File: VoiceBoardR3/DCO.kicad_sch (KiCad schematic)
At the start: 74 parts, among them Q201 BC857, Q202 BC857, U201 TL074, U202 TL074, U203 MCP4451-104E-ST, U204 TL074, U205 MCP4451-104E-ST, U206 TL072

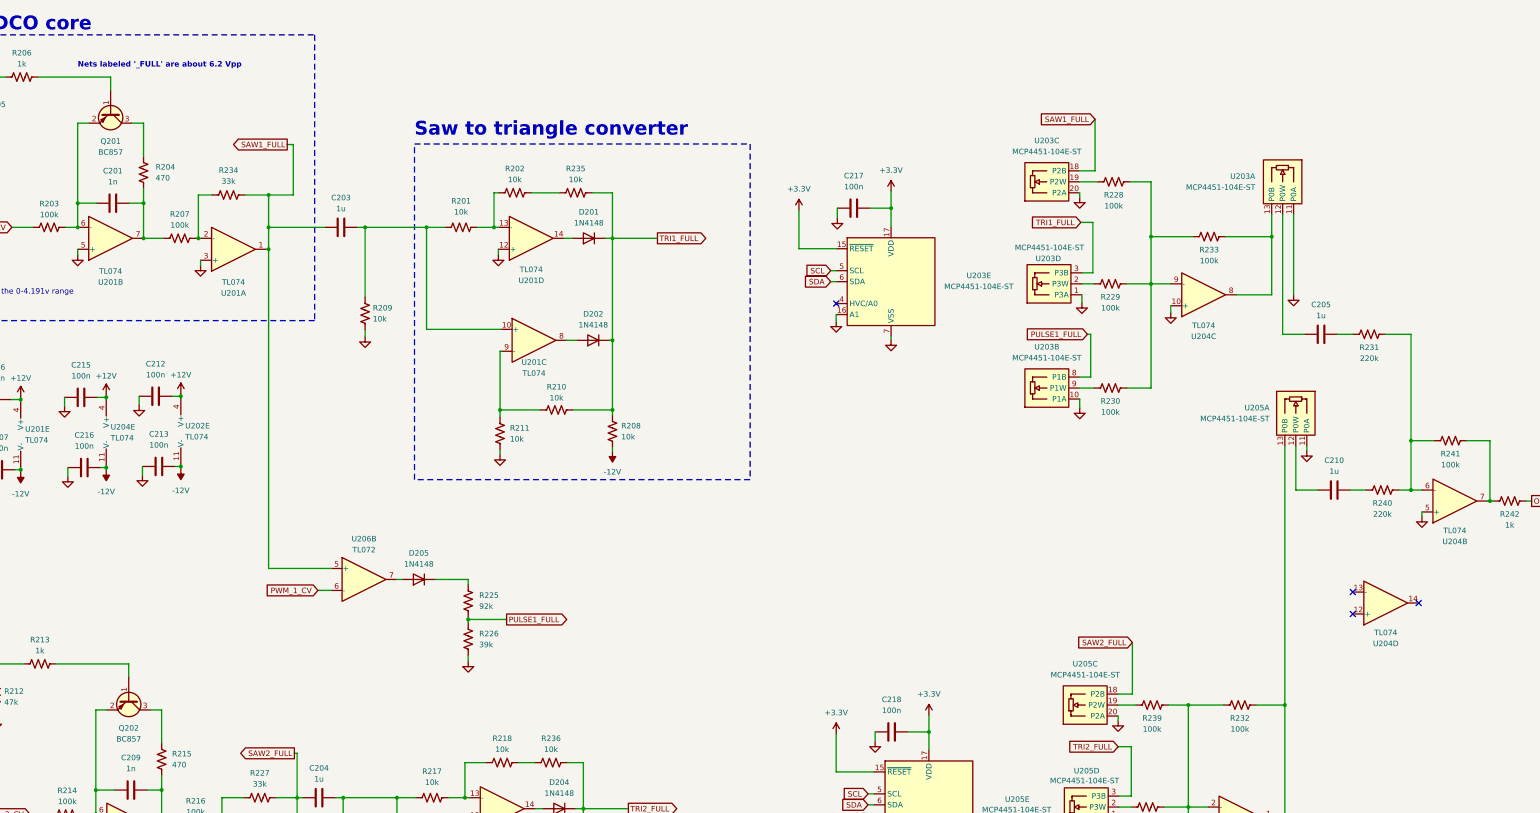
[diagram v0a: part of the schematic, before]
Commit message: updated to kicad 8
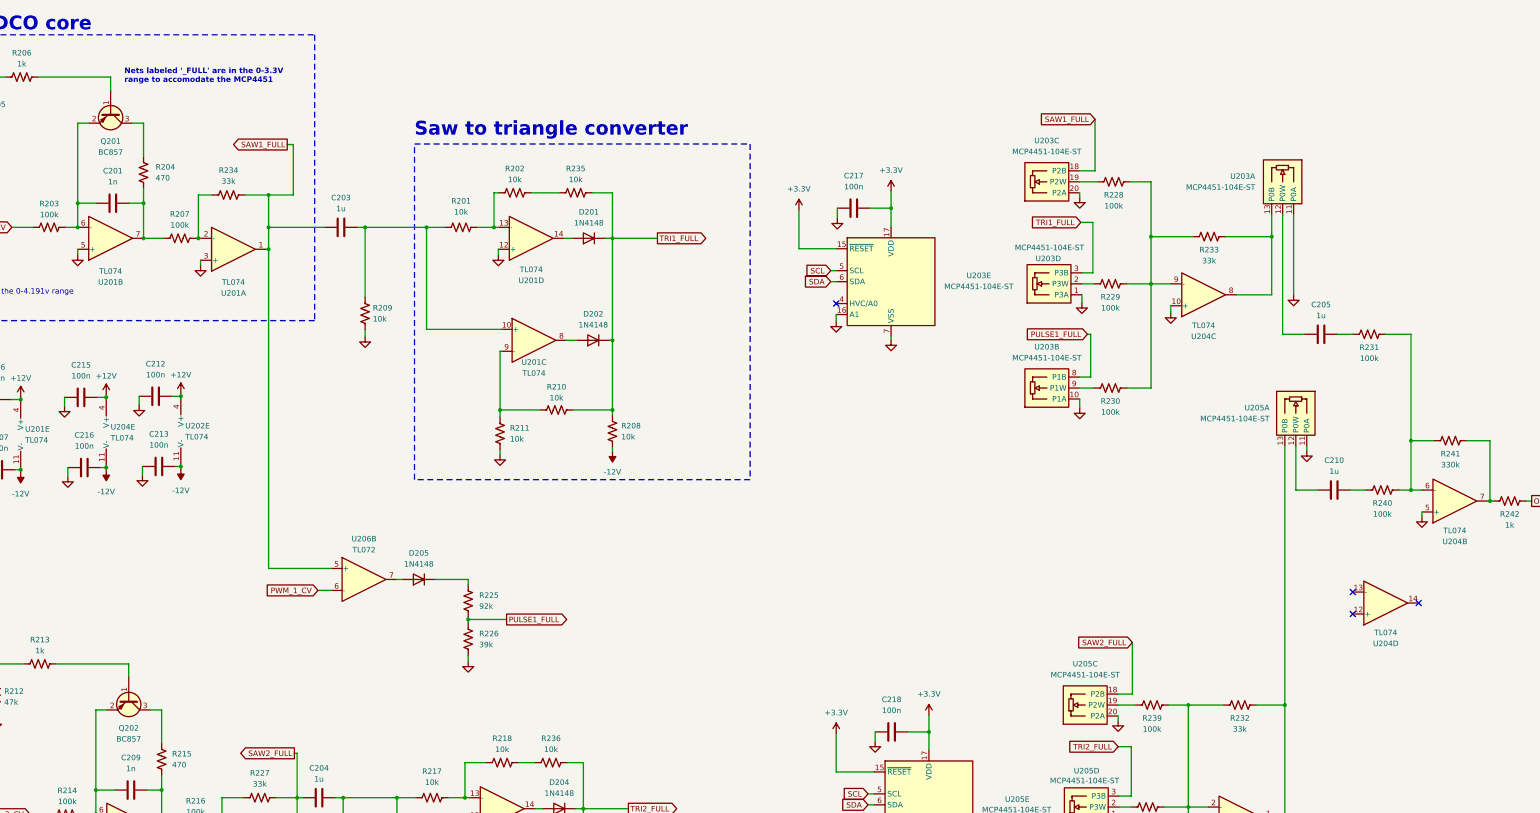
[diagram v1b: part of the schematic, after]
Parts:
- R231, R240: value 220k -> 100k
- R232, R233: value 100k -> 33k
- R241: value 100k -> 330k
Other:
- note added: "Nets labeled '_FULL' are in the 0-3.3V range to accomodate the MCP4451"
- note removed: "Nets labeled '_FULL' are about 6.2 Vpp"
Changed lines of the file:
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@@
     (effects (font (size 1.27 1.27)) (justify left bottom))
   )
-  (text "Nets labeled '_FULL' are about 6.2 Vpp" (at 59.436 25.908 0)
+  (text "Nets labeled '_FULL' are in the 0-3.3V \nrange to accomodate the MCP4451"
+    (at 70.231 29.464 0)
     (effects (font (size 1.27 1.27) (thickness 0.254) bold) (justify left bottom))
   )
@@
       (effects (font (size 1.27 1.27)))
     )
-    (property "Value" "100k" (at 377.317 117.729 90)
+    (property "Value" "330k" (at 377.317 117.729 90)
       (effects (font (size 1.27 1.27)))
     )
@@
       (effects (font (size 1.27 1.27)))
     )
-    (property "Value" "220k" (at 361.569 129.159 90)
+    (property "Value" "100k" (at 361.569 129.159 90)
       (effects (font (size 1.27 1.27)))
     )
@@
       (effects (font (size 1.27 1.27)))
     )
-    (property "Value" "220k" (at 358.521 93.091 90)
+    (property "Value" "100k" (at 358.521 93.091 90)
       (effects (font (size 1.27 1.27)))
     )
@@
       (effects (font (size 1.27 1.27)))
     )
-    (property "Value" "100k" (at 328.549 178.943 90)
+    (property "Value" "33k" (at 328.549 178.943 90)
       (effects (font (size 1.27 1.27)))
     )
@@
       (effects (font (size 1.27 1.27)))
     )
-    (property "Value" "100k" (at 321.437 70.485 90)
+    (property "Value" "33k" (at 321.437 70.485 90)
       (effects (font (size 1.27 1.27)))
     )

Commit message: separate power supply board
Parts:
- removed C219, C220: 100n, Capacitor_SMD:C_0805_2012Metric, symbol Device:C
- removed U206: TL072, Package_SO:SOIC-8_3.9x4.9mm_P1.27mm, symbol Amplifier_Operational:TL072
- added C211, C214: 1u, Capacitor_SMD:C_0805_2012Metric, symbol Device:C
- added R220: 100k, Resistor_SMD:R_0805_2012Metric, symbol Device:R_US
- added R244: 10k, Resistor_SMD:R_0805_2012Metric, symbol Device:R_US
- added R245: 56k, Resistor_SMD:R_0805_2012Metric, symbol Device:R_US
- added R246: 470, Resistor_SMD:R_0805_2012Metric, symbol Device:R_US
- added SAW1, TRI1, TRI2: SAW1_DC, TestPoint:TestPoint_THTPad_D1.0mm_Drill0.5mm, symbol Connector:TestPoint
- added SAW2: SAW2_DC, TestPoint:TestPoint_THTPad_D1.0mm_Drill0.5mm, symbol Connector:TestPoint
- added U206: TL074, Package_SO:SOIC-14_3.9x8.7mm_P1.27mm, symbol Amplifier_Operational:TL074
- C205, C210: value 1u -> 100n
- Q201, Q202: footprint PCM_Package_TO_SOT_SMD_AKL:SOT-23 -> PCM_4ms_Package_SOT:SOT-23
- R201, R202, R203, R204, R205, R206, R207, R208, R209, R210, R211, R212, R213, R214, R215, R216, R217, R218, R219, R221, R222, R223, R224, R225, R226, R227, R228, R229, R230, R231, R232, R233, R234, R235, R236, R237, R238, R239, R240, R243: footprint PCM_Resistor_SMD_AKL:R_0805_2012Metric -> Resistor_SMD:R_0805_2012Metric
- R241: value 330k -> 100k; footprint PCM_Resistor_SMD_AKL:R_0805_2012Metric -> Resistor_SMD:R_0805_2012Metric
- R242: value 1k -> 10k; footprint PCM_Resistor_SMD_AKL:R_0805_2012Metric -> Resistor_SMD:R_0805_2012Metric
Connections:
- net +12V: now also C205.2, U206.4 (V+)
- net -12V: now also C210.2, U206.11 (V-)
- net GND: now also C205.1, C210.1, U204.12 (+), U206.3 (+)
- net OSC_MIX: now also R246.2; no longer R242.2
- net PWM_1_CV: now also U206.5 (+)
- net PWM_2_CV: now also U206.10 (+)
- net SAW1_FULL: now also SAW1.1, U206.6 (-)
- net SAW2_FULL: now also SAW2.1, U206.9 (-)
- net TRI1_FULL: now also TRI1.1
- net TRI2_FULL: now also TRI2.1
- net at R228.2, R229.2, R230.2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: now also U204.13 (-); no longer U204.9 (-)
- net at R240.2, R241.1: now also U204.9 (-); no longer R231.2, U204.6 (-)
- net at D205.2 (A): now also U206.7
- net at U203.12 (P0W): now also C214.1; no longer C205.1
- net at U204.14: now also R233.2, R240.1
- net at U205.12 (P0W): now also C211.1; no longer C210.1
- net at R232.2, U204.1: now also R220.1; no longer U205.13 (P0B)
- net at R231.1: now also U204.6 (-), R220.2; no longer C205.2
- net at D206.2 (A): now also U206.8
- new net: C211.2, R244.1
- new net: R245.2, R246.1, U206.1
- new net: R242.2, R244.2, R245.1, U206.2 (-)
- new net: R231.2, U203.13 (P0B), U204.7
- new net: C214.2, R242.1
- new net: R241.2, U204.8, U205.13 (P0B)
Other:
- note added: "Mixer"
- note added: "NOTE: we need to invert the summed signal again here to be within the range of the digital pot"
- note added: "The decouplig caps and inverting amp here give us a 6Vpp AC signal"
- moved on the sheet: C217, C218, R228, R229, R230, R232, R233, R237, R238, R239, U203A, U203B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

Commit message: Power Supply rev2
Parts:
- R223: value 39k -> 47k
- R224: value 92k -> 100k
- R226: value 39k -> 100k
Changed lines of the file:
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@@
 		(fields_autoplaced yes)
 		(property "Reference" "R224"
-			(at 146.558 258.572 0)
+			(at 146.05 258.5719 0)
 			(effects
 				(font
@@
 			)
 		)
-		(property "Value" "92k"
-			(at 146.558 261.112 0)
+		(property "Value" "100k"
+			(at 146.05 261.1119 0)
 			(effects
 				(font
@@
 		(fields_autoplaced yes)
 		(property "Reference" "R226"
-			(at 152.4 156.972 0)
+			(at 152.4 156.9719 0)
 			(effects
 				(font
@@
 			)
 		)
-		(property "Value" "39k"
-			(at 152.4 159.512 0)
+		(property "Value" "100k"
+			(at 152.4 159.5119 0)
 			(effects
 				(font
@@
 		(fields_autoplaced yes)
 		(property "Reference" "R223"
-			(at 146.558 267.462 0)
+			(at 146.05 267.4619 0)
 			(effects
 				(font
@@
 			)
 		)
-		(property "Value" "39k"
-			(at 146.558 270.002 0)
+		(property "Value" "47k"
+			(at 146.05 270.0019 0)
 			(effects
 				(font
